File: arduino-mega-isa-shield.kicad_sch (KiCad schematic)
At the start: 11 parts, among them J1 EBC49DCWN-S420, J2 JST VH 1x6, U1 ICS501, Y1 3.579545MHZ

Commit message: Reverse LA17-LA23 for sequential port access, re-route board
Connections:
- net LA17: now also XA1.A8; no longer XA1.A14
- net LA18: now also XA1.A9; no longer XA1.A13
- net LA19: now also XA1.A10; no longer XA1.A12
- net LA21: now also XA1.A12; no longer XA1.A10
- net LA22: now also XA1.A13; no longer XA1.A9
- net LA23: now also XA1.A14; no longer XA1.A8
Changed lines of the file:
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@@
     (effects (font (size 1.27 1.27)) (justify left bottom))
   )
-  (label "LA23" (at 177.165 74.93 0)
+  (label "LA23" (at 177.165 59.69 0)
     (effects (font (size 1.27 1.27)) (justify left bottom))
   )
@@
     (effects (font (size 1.27 1.27)) (justify right bottom))
   )
-  (label "LA19" (at 177.165 64.77 0)
+  (label "LA19" (at 177.165 69.85 0)
     (effects (font (size 1.27 1.27)) (justify left bottom))
   )
@@
     (effects (font (size 1.27 1.27)) (justify right bottom))
   )
-  (label "LA22" (at 177.165 72.39 0)
+  (label "LA22" (at 177.165 62.23 0)
     (effects (font (size 1.27 1.27)) (justify left bottom))
   )
@@
     (effects (font (size 1.27 1.27)) (justify left bottom))
   )
-  (label "LA21" (at 177.165 69.85 0)
+  (label "LA21" (at 177.165 64.77 0)
     (effects (font (size 1.27 1.27)) (justify left bottom))
   )
@@
     (effects (font (size 1.27 1.27)) (justify right bottom))
   )
-  (label "LA17" (at 177.165 59.69 0)
+  (label "LA17" (at 177.165 74.93 0)
     (effects (font (size 1.27 1.27)) (justify left bottom))
   )
@@
     (effects (font (size 1.27 1.27)) (justify right bottom))
   )
-  (label "LA18" (at 177.165 62.23 0)
+  (label "LA18" (at 177.165 72.39 0)
     (effects (font (size 1.27 1.27)) (justify left bottom))
   )
@@
   (symbol (lib_id "power:+5V") (at 98.425 54.61 180) (unit 1)
     (in_bom yes) (on_board yes) (fields_autoplaced)
-    (property "Reference" "#PWR?" (id 0) (at 98.425 50.8 0)
+    (property "Reference" "#PWR0118" (id 0) (at 98.425 50.8 0)
       (effects (font (size 1.27 1.27)) hide)
     )
@@
   (symbol (lib_id "power:GND") (at 88.265 41.275 0) (unit 1)
     (in_bom yes) (on_board yes) (fields_autoplaced)
-    (property "Reference" "#PWR?" (id 0) (at 88.265 47.625 0)
+    (property "Reference" "#PWR0117" (id 0) (at 88.265 47.625 0)
       (effects (font (size 1.27 1.27)) hide)
     )
@@
   (symbol (lib_id "power:GND") (at 78.74 41.275 0) (unit 1)
     (in_bom yes) (on_board yes) (fields_autoplaced)
-    (property "Reference" "#PWR?" (id 0) (at 78.74 47.625 0)
+    (property "Reference" "#PWR0116" (id 0) (at 78.74 47.625 0)
       (effects (font (size 1.27 1.27)) hide)
     )
@@
   (symbol (lib_id "power:GND") (at 111.125 48.26 0) (unit 1)
     (in_bom yes) (on_board yes) (fields_autoplaced)
-    (property "Reference" "#PWR?" (id 0) (at 111.125 54.61 0)
+    (property "Reference" "#PWR0119" (id 0) (at 111.125 54.61 0)
       (effects (font (size 1.27 1.27)) hide)
     )
@@
       (reference "#PWR0115") (unit 1) (value "+12V") (footprint "")
     )
+    (path "/d448079f-1000-4af8-91cc-a524284b08b6"
+      (reference "#PWR0116") (unit 1) (value "GND") (footprint "")
+    )
+    (path "/48275625-fa15-4251-ab39-f67d933a2e39"
+      (reference "#PWR0117") (unit 1) (value "GND") (footprint "")
+    )
     (path "/1a21c0e6-1c0e-48d8-a7bc-903ed42743aa"
-      (reference "#PWR?") (unit 1) (value "+5V") (footprint "")
-    )
-    (path "/48275625-fa15-4251-ab39-f67d933a2e39"
-      (reference "#PWR?") (unit 1) (value "GND") (footprint "")
-    )
-    (path "/d448079f-1000-4af8-91cc-a524284b08b6"
-      (reference "#PWR?") (unit 1) (value "GND") (footprint "")
+      (reference "#PWR0118") (unit 1) (value "+5V") (footprint "")
     )
     (path "/e8ac3a12-c7a0-43b7-8412-d0c62382e2e5"
-      (reference "#PWR?") (unit 1) (value "GND") (footprint "")
+      (reference "#PWR0119") (unit 1) (value "GND") (footprint "")
     )
     (path "/639f04ee-b905-458e-a991-f5f5fed4bace"

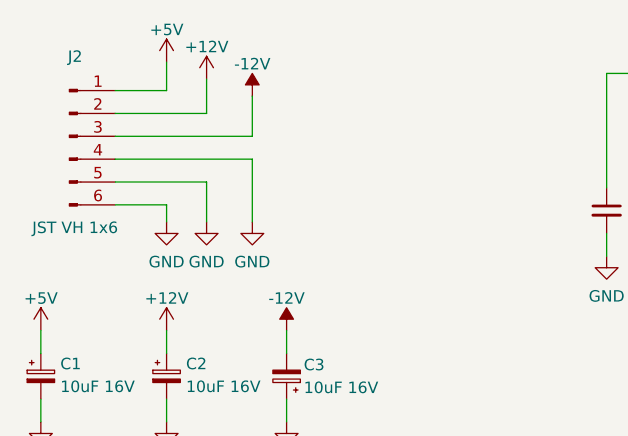
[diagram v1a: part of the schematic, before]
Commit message: Rework board
lmao the ISA connector pinout was flipped
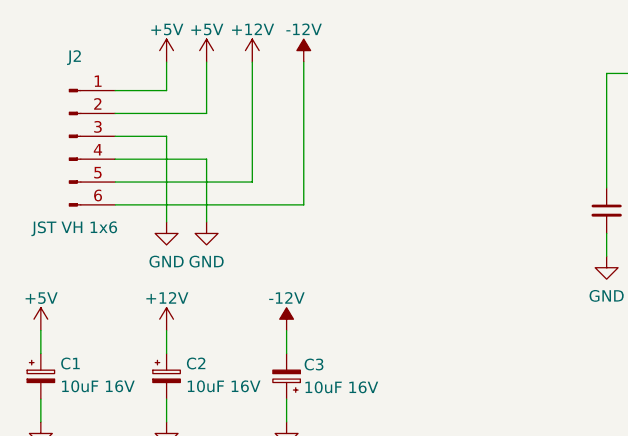
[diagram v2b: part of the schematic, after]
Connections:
- net +12V: now also J2.5 (Pin_5); no longer J2.2 (Pin_2)
- net +5V: now also J2.2 (Pin_2)
- net -12V: now also J2.6 (Pin_6); no longer J2.3 (Pin_3)
- net GND: now also J2.3 (Pin_3); no longer J2.5 (Pin_5), J2.6 (Pin_6)
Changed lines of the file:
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@@
+    (stroke (width 0) (type default) (color 0 0 0 0))
+  )
+  (wire (pts (xy 34.29 30.48) (xy 34.29 37.465))
     (stroke (width 0) (type default) (color 0 0 0 0))
   )
@@
     (stroke (width 0) (type default) (color 0 0 0 0))
   )
+  (wire (pts (xy 24.13 30.48) (xy 34.29 30.48))
+    (stroke (width 0) (type default) (color 0 0 0 0))
+  )
   (wire (pts (xy 29.845 49.53) (xy 29.845 52.07))
     (stroke (width 0) (type default) (color 0 0 0 0))
@@
     (stroke (width 0) (type default) (color 0 0 0 0))
   )
+  (wire (pts (xy 29.845 27.94) (xy 29.845 37.465))
+    (stroke (width 0) (type default) (color 0 0 0 0))
+  )
   (wire (pts (xy 173.355 40.005) (xy 177.165 40.005))
     (stroke (width 0) (type default) (color 0 0 0 0))
@@
     (stroke (width 0) (type default) (color 0 0 0 0))
   )
-  (wire (pts (xy 39.37 30.48) (xy 39.37 37.465))
-    (stroke (width 0) (type default) (color 0 0 0 0))
-  )
   (wire (pts (xy 172.72 151.765) (xy 177.165 151.765))
     (stroke (width 0) (type default) (color 0 0 0 0))
   )
+  (wire (pts (xy 34.29 19.685) (xy 34.29 25.4))
+    (stroke (width 0) (type default) (color 0 0 0 0))
+  )
   (wire (pts (xy 172.72 67.31) (xy 177.165 67.31))
     (stroke (width 0) (type default) (color 0 0 0 0))
@@
     (stroke (width 0) (type default) (color 0 0 0 0))
   )
-  (wire (pts (xy 34.29 21.59) (xy 34.29 25.4))
-    (stroke (width 0) (type default) (color 0 0 0 0))
-  )
-  (wire (pts (xy 24.13 35.56) (xy 29.845 35.56))
-    (stroke (width 0) (type default) (color 0 0 0 0))
-  )
   (wire (pts (xy 100.965 40.64) (xy 100.965 46.355))
     (stroke (width 0) (type default) (color 0 0 0 0))
   )
-  (wire (pts (xy 29.845 35.56) (xy 29.845 37.465))
-    (stroke (width 0) (type default) (color 0 0 0 0))
-  )
   (wire (pts (xy 274.32 69.215) (xy 277.495 69.215))
     (stroke (width 0) (type default) (color 0 0 0 0))
@@
     (stroke (width 0) (type default) (color 0 0 0 0))
   )
+  (wire (pts (xy 45.085 19.685) (xy 45.085 35.56))
+    (stroke (width 0) (type default) (color 0 0 0 0))
+  )
   (wire (pts (xy 172.72 74.93) (xy 177.165 74.93))
     (stroke (width 0) (type default) (color 0 0 0 0))
@@
     (stroke (width 0) (type default) (color 0 0 0 0))
   )
+  (wire (pts (xy 24.13 35.56) (xy 45.085 35.56))
+    (stroke (width 0) (type default) (color 0 0 0 0))
+  )
   (wire (pts (xy 273.05 34.925) (xy 264.795 34.925))
     (stroke (width 0) (type default) (color 0 0 0 0))
@@
     (stroke (width 0) (type default) (color 0 0 0 0))
   )
-  (wire (pts (xy 24.13 30.48) (xy 39.37 30.48))
+  (wire (pts (xy 39.37 19.685) (xy 39.37 33.02))
     (stroke (width 0) (type default) (color 0 0 0 0))
   )
@@
     (stroke (width 0) (type default) (color 0 0 0 0))
   )
+  (wire (pts (xy 24.13 33.02) (xy 39.37 33.02))
+    (stroke (width 0) (type default) (color 0 0 0 0))
+  )
   (wire (pts (xy 24.13 22.86) (xy 29.845 22.86))
     (stroke (width 0) (type default) (color 0 0 0 0))
@@
     (stroke (width 0) (type default) (color 0 0 0 0))
   )
-  (wire (pts (xy 24.13 33.02) (xy 34.29 33.02))
-    (stroke (width 0) (type default) (color 0 0 0 0))
-  )
   (wire (pts (xy 274.32 66.675) (xy 277.495 66.675))
     (stroke (width 0) (type default) (color 0 0 0 0))
@@
     (stroke (width 0) (type default) (color 0 0 0 0))
   )
-  (wire (pts (xy 39.37 23.495) (xy 39.37 27.94))
-    (stroke (width 0) (type default) (color 0 0 0 0))
-  )
   (wire (pts (xy 172.72 106.045) (xy 177.165 106.045))
     (stroke (width 0) (type default) (color 0 0 0 0))
@@
     (stroke (width 0) (type default) (color 0 0 0 0))
   )
-  (wire (pts (xy 24.13 27.94) (xy 39.37 27.94))
+  (wire (pts (xy 24.13 27.94) (xy 29.845 27.94))
     (stroke (width 0) (type default) (color 0 0 0 0))
   )
@@
   )
   (wire (pts (xy 111.125 46.355) (xy 122.555 46.355))
-    (stroke (width 0) (type default) (color 0 0 0 0))
-  )
-  (wire (pts (xy 34.29 33.02) (xy 34.29 37.465))
     (stroke (width 0) (type default) (color 0 0 0 0))
   )
@@
     (pin "1")
   )
-  (symbol (lib_id "power:+12V") (at 34.29 21.59 0) (unit 1)
-    (in_bom yes) (on_board yes) (fields_autoplaced)
-    (property "Reference" "#PWR0101" (id 0) (at 34.29 25.4 0)
-      (effects (font (size 1.27 1.27)) hide)
-    )
-    (property "Value" "+12V" (id 1) (at 34.29 18.0142 0))
-    (property "Footprint" "" (id 2) (at 34.29 21.59 0)
-      (effects (font (size 1.27 1.27)) hide)
-    )
-    (property "Datasheet" "" (id 3) (at 34.29 21.59 0)
+  (symbol (lib_id "power:+12V") (at 39.37 19.685 0) (unit 1)
+    (in_bom yes) (on_board yes) (fields_autoplaced)
+    (property "Reference" "#PWR0101" (id 0) (at 39.37 23.495 0)
+      (effects (font (size 1.27 1.27)) hide)
+    )
+    (property "Value" "+12V" (id 1) (at 39.37 16.1092 0))
+    (property "Footprint" "" (id 2) (at 39.37 19.685 0)
+      (effects (font (size 1.27 1.27)) hide)
+    )
+    (property "Datasheet" "" (id 3) (at 39.37 19.685 0)
+      (effects (font (size 1.27 1.27)) hide)
+    )
+    (pin "1")
+  )
+  (symbol (lib_id "power:+5V") (at 34.29 19.685 0) (unit 1)
+    (in_bom yes) (on_board yes)
+    (property "Reference" "#PWR?" (id 0) (at 34.29 23.495 0)
+      (effects (font (size 1.27 1.27)) hide)
+    )
+    (property "Value" "+5V" (id 1) (at 34.29 16.1092 0))
+    (property "Footprint" "" (id 2) (at 34.29 19.685 0)
+      (effects (font (size 1.27 1.27)) hide)
+    )
+    (property "Datasheet" "" (id 3) (at 34.29 19.685 0)
       (effects (font (size 1.27 1.27)) hide)
     )
@@
     (pin "6")
   )
-  (symbol (lib_id "power:-12V") (at 39.37 23.495 0) (unit 1)
-    (in_bom yes) (on_board yes) (fields_autoplaced)
-    (property "Reference" "#PWR0103" (id 0) (at 39.37 20.955 0)
-      (effects (font (size 1.27 1.27)) hide)
-    )
-    (property "Value" "-12V" (id 1) (at 39.37 19.9192 0))
-    (property "Footprint" "" (id 2) (at 39.37 23.495 0)
-      (effects (font (size 1.27 1.27)) hide)
-    )
-    (property "Datasheet" "" (id 3) (at 39.37 23.495 0)
+  (symbol (lib_id "power:-12V") (at 45.085 19.685 0) (unit 1)
+    (in_bom yes) (on_board yes) (fields_autoplaced)
+    (property "Reference" "#PWR0103" (id 0) (at 45.085 17.145 0)
+      (effects (font (size 1.27 1.27)) hide)
+    )
+    (property "Value" "-12V" (id 1) (at 45.085 16.1092 0))
+    (property "Footprint" "" (id 2) (at 45.085 19.685 0)
+      (effects (font (size 1.27 1.27)) hide)
+    )
+    (property "Datasheet" "" (id 3) (at 45.085 19.685 0)
       (effects (font (size 1.27 1.27)) hide)
     )
@@
     (pin "1")
   )
-  (symbol (lib_id "power:GND") (at 39.37 37.465 0) (unit 1)
-    (in_bom yes) (on_board yes) (fields_autoplaced)
-    (property "Reference" "#PWR0105" (id 0) (at 39.37 43.815 0)
-      (effects (font (size 1.27 1.27)) hide)
-    )
-    (property "Value" "GND" (id 1) (at 39.37 41.9084 0))
-    (property "Footprint" "" (id 2) (at 39.37 37.465 0)
-      (effects (font (size 1.27 1.27)) hide)
-    )
-    (property "Datasheet" "" (id 3) (at 39.37 37.465 0)
-      (effects (font (size 1.27 1.27)) hide)
-    )
-    (pin "1")
-  )
   (symbol (lib_id "PCM_arduino-library:Arduino_Mega2560_Shield") (at 55.245 131.445 0) (unit 1)
     (in_bom yes) (on_board yes) (fields_autoplaced)
@@
       (reference "#PWR0104") (unit 1) (value "GND") (footprint "")
     )
-    (path "/ebb92501-37a6-481a-a2f4-68ed04d34940"
-      (reference "#PWR0105") (unit 1) (value "GND") (footprint "")
-    )
     (path "/38fac0f7-fd2e-4310-9091-be376b4976b3"
       (reference "#PWR0106") (unit 1) (value "GND") (footprint "")
@@
       (reference "#PWR0119") (unit 1) (value "GND") (footprint "")
     )
+    (path "/1944d399-3f40-4b51-a42f-3b429e406943"
+      (reference "#PWR?") (unit 1) (value "+5V") (footprint "")
+    )
     (path "/639f04ee-b905-458e-a991-f5f5fed4bace"
